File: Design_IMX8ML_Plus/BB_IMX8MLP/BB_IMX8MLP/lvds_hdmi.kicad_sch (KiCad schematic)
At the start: 4 parts, among them J15 LVDS0, J16 LVDS0, J7 HDMI_A, U2 HDMI2C1-14HDS

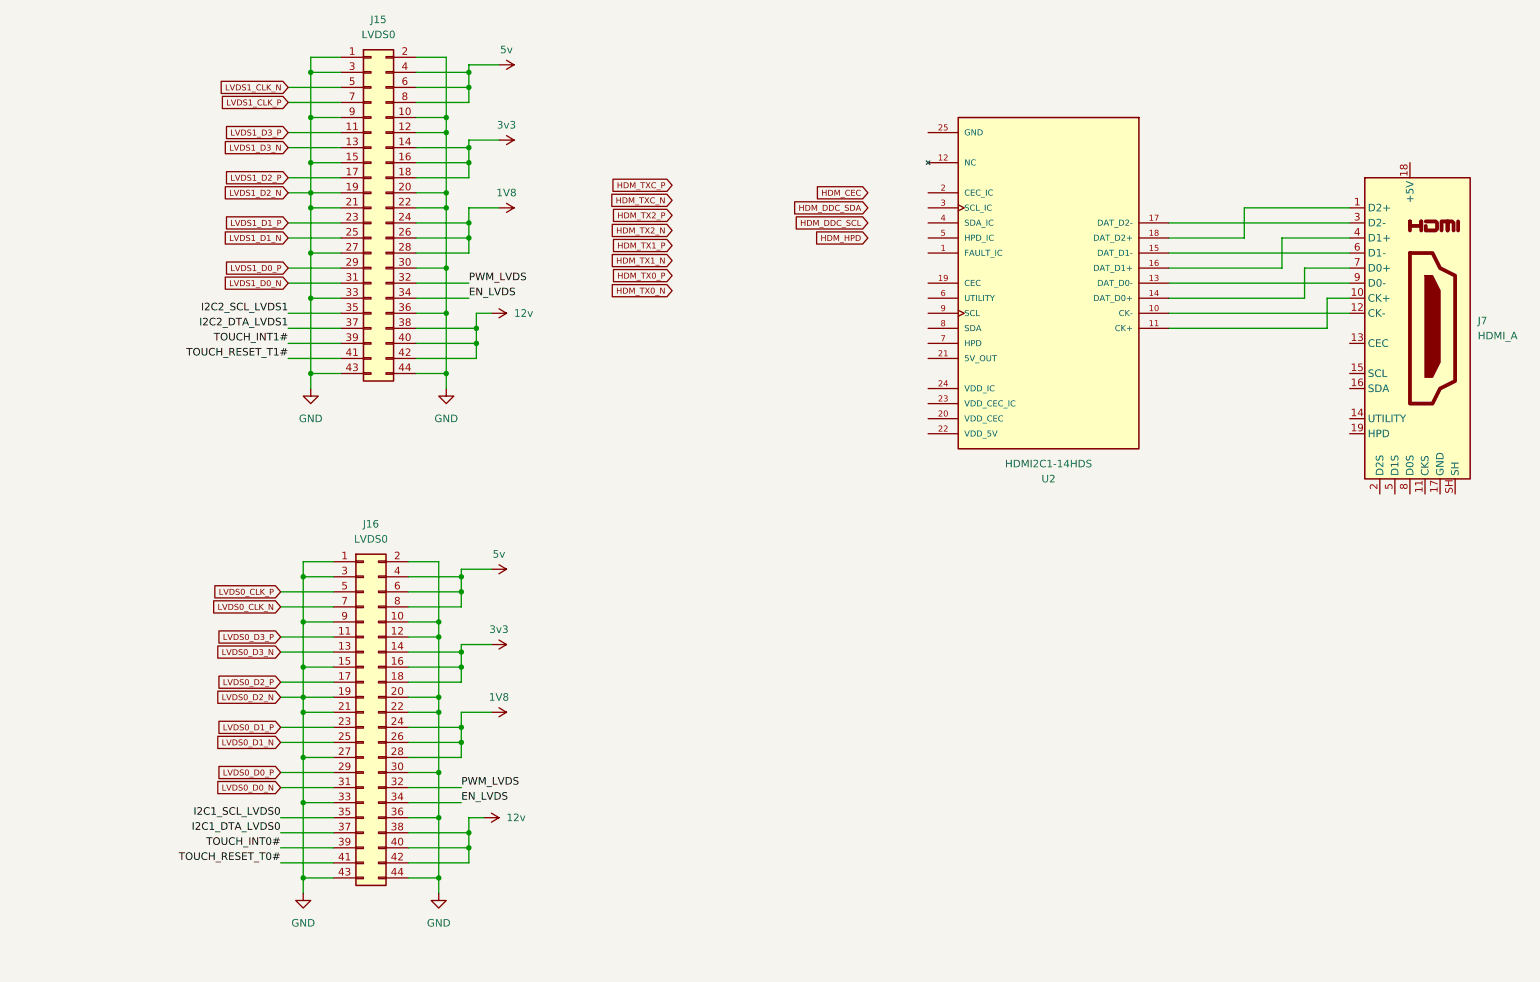
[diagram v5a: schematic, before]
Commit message: reorganization of the componentes
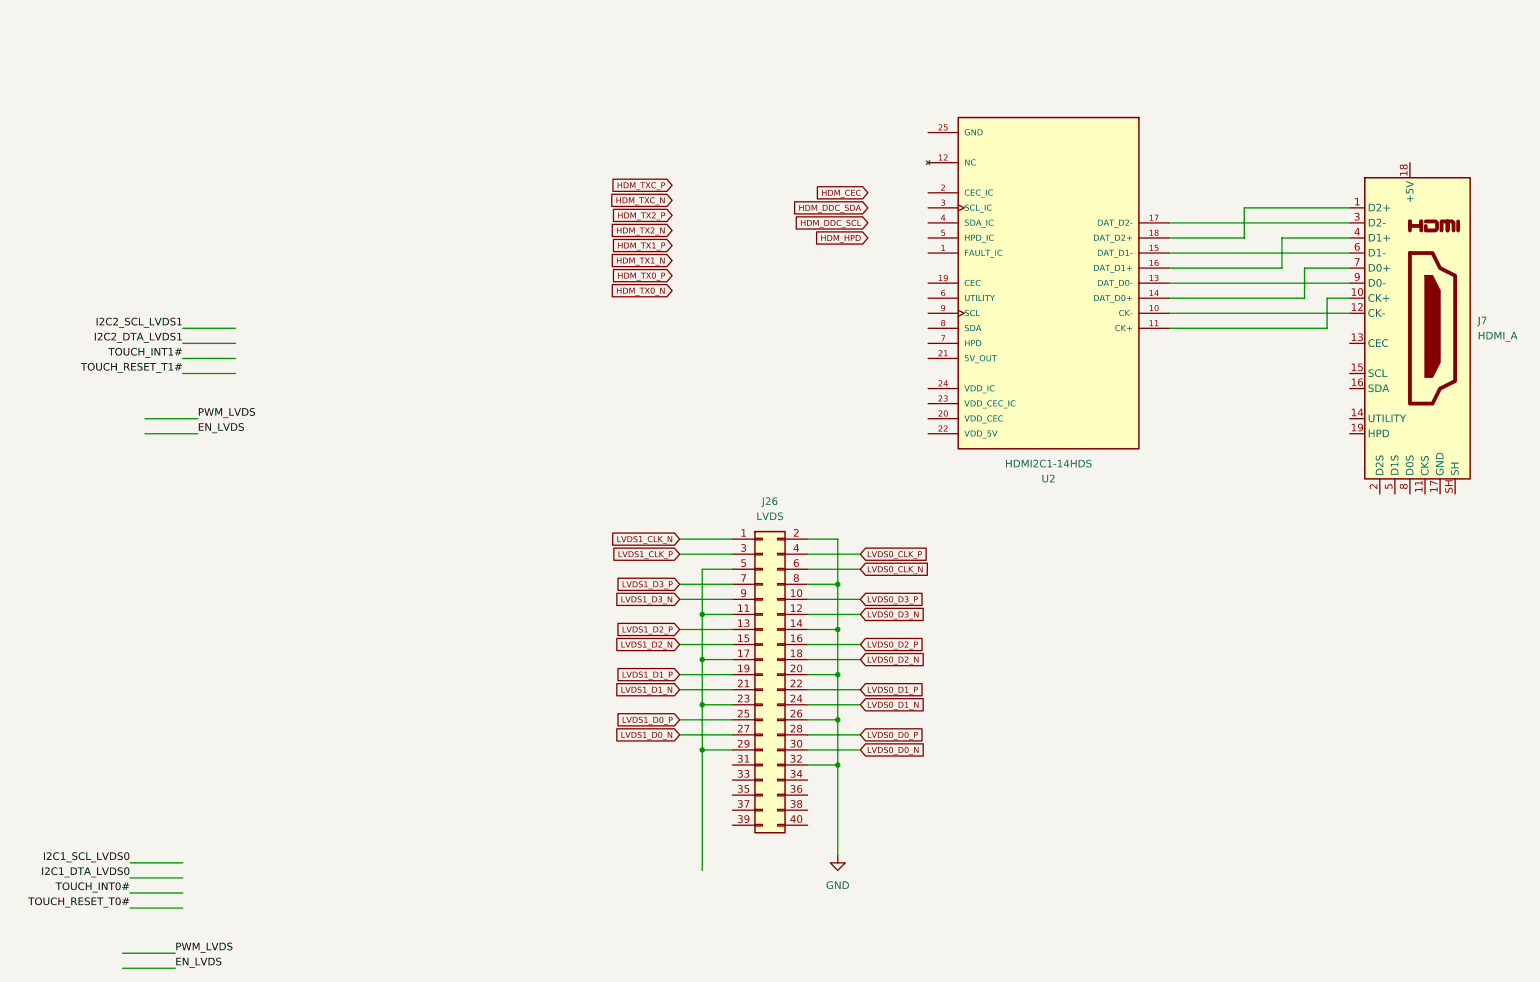
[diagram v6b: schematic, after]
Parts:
- removed J15, J16: LVDS0, symbol Connector_Generic:Conn_02x22_Odd_Even
- added J26: LVDS, Connector_PinHeader_1.00mm:PinHeader_2x20_P1.00mm_Vertical_SMD, symbol Connector_Generic:Conn_02x20_Odd_Even
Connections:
- net GND: now also J26.14 (Pin_14), J26.2 (Pin_2), J26.20 (Pin_20), J26.26 (Pin_26), J26.32 (Pin_32), J26.8 (Pin_8)
- net LVDS0_CLK_N: now also J26.6 (Pin_6)
- net LVDS0_CLK_P: now also J26.4 (Pin_4)
- net LVDS0_D0_N: now also J26.30 (Pin_30)
- net LVDS0_D0_P: now also J26.28 (Pin_28)
- net LVDS0_D1_N: now also J26.24 (Pin_24)
- net LVDS0_D1_P: now also J26.22 (Pin_22)
- net LVDS0_D2_P: now also J26.16 (Pin_16)
- net LVDS0_D3_N: now also J26.12 (Pin_12)
- net LVDS0_D3_P: now also J26.10 (Pin_10)
- net LVDS1_CLK_N: now also J26.1 (Pin_1)
- net LVDS1_CLK_P: now also J26.3 (Pin_3)
- net LVDS1_D0_N: now also J26.27 (Pin_27)
- net LVDS1_D0_P: now also J26.25 (Pin_25)
- net LVDS1_D1_N: now also J26.21 (Pin_21)
- net LVDS1_D1_P: now also J26.19 (Pin_19)
- net LVDS1_D2_P: now also J26.13 (Pin_13)
- net LVDS1_D3_N: now also J26.9 (Pin_9)
- net LVDS1_D3_P: now also J26.7 (Pin_7)
- new net: J26.11 (Pin_11), J26.17 (Pin_17), J26.23 (Pin_23), J26.29 (Pin_29), J26.5 (Pin_5)
- new net LVDS0_D2_N: J26.18 (Pin_18)
- new net LVDS1_D2_N: J26.15 (Pin_15)

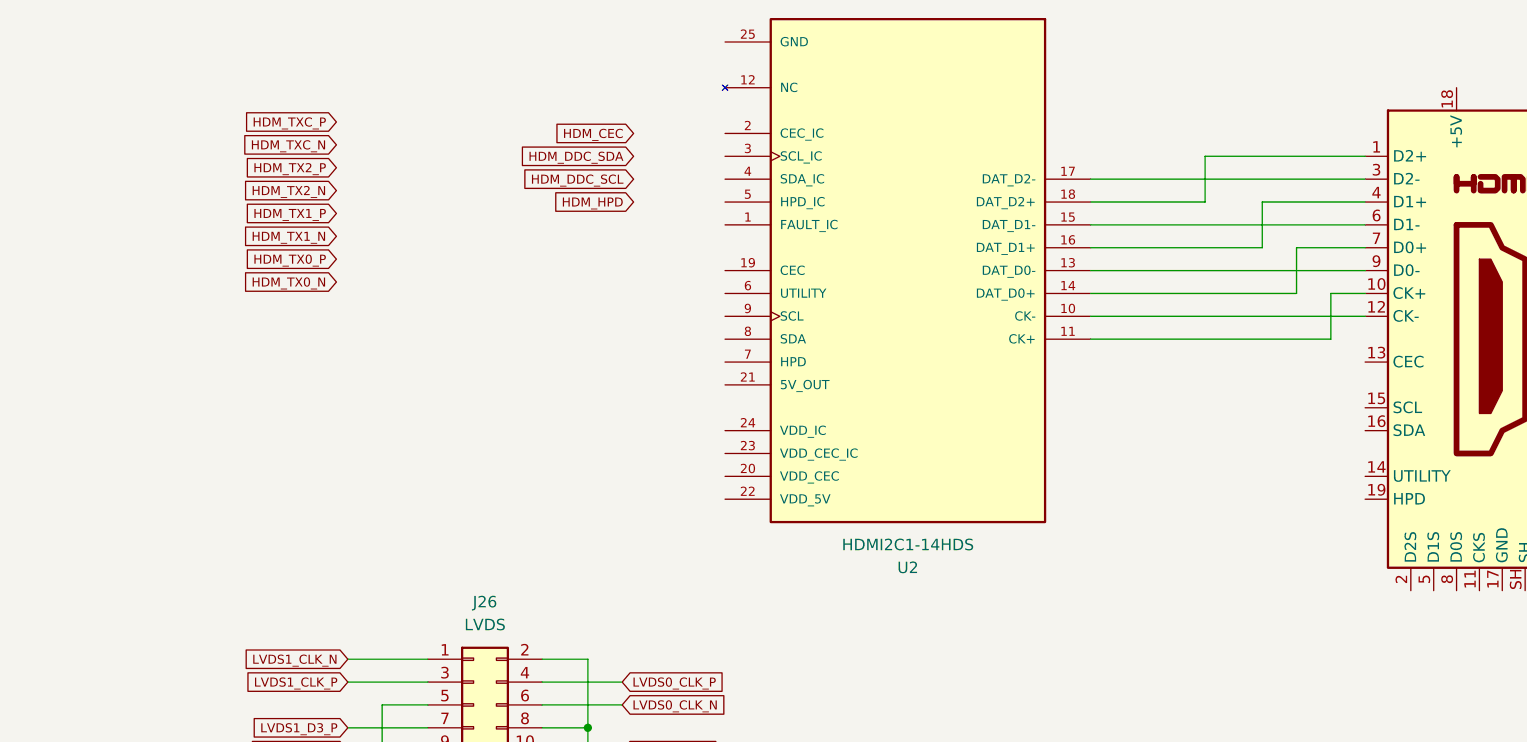
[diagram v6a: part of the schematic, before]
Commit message: Board base resize
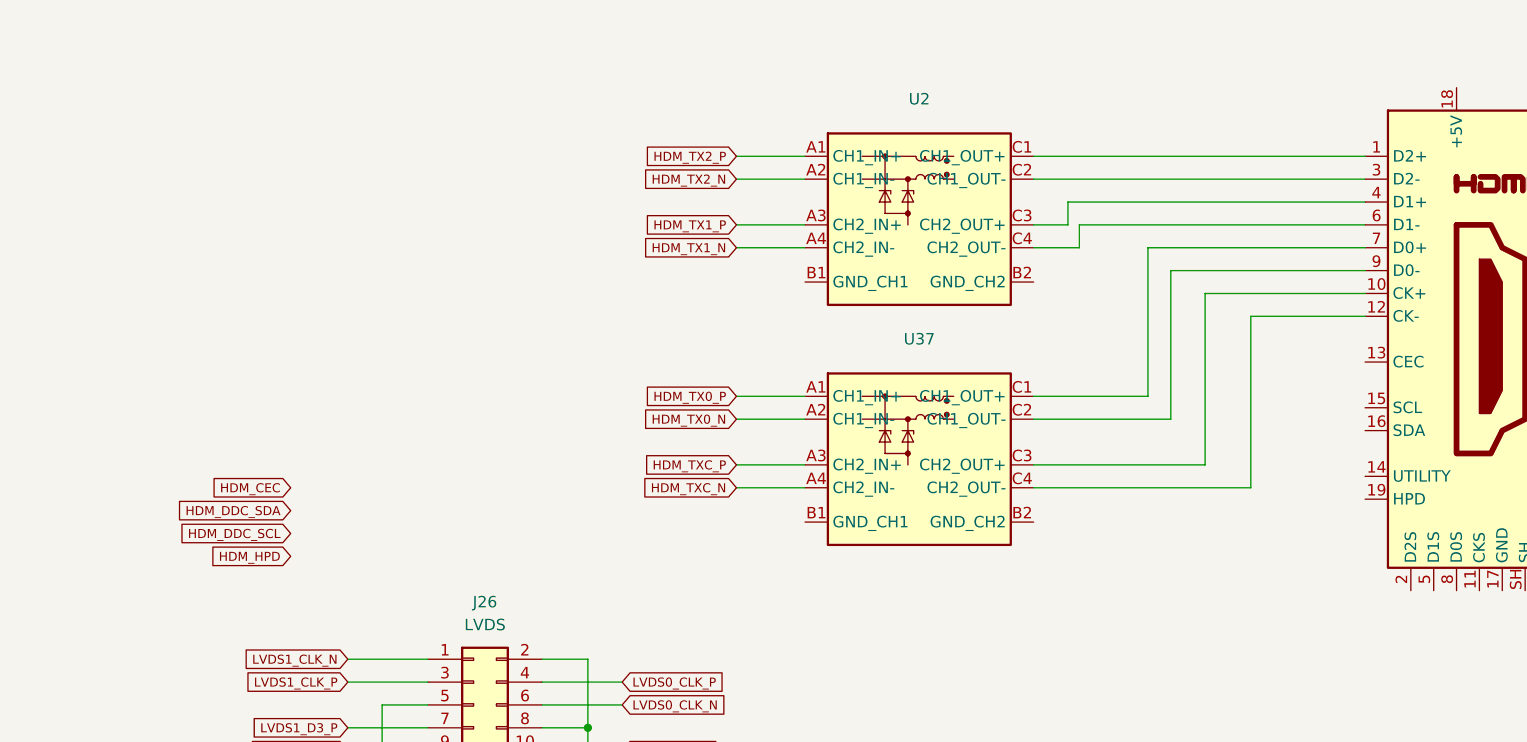
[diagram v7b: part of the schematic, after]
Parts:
- removed U2: HDMI2C1-14HDS, Package_DFN_QFN:VQFN-24-1EP_4x4mm_P0.5mm_EP2.5x2.5mm, symbol HDMI2C1-14HDS:HDMI2C1-14HDS
- added U2, U37: ~, _W_SBC:WLCSP10_4-2-4_NEX, symbol _W_MX8M:PCMF2HDMI12S
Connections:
- net HDM_TX0_N: now also U37.A2 (CH1_IN-)
- net HDM_TX0_P: now also U37.A1 (CH1_IN+)
- net HDM_TX1_N: now also U2.A4 (CH2_IN-)
- net HDM_TX1_P: now also U2.A3 (CH2_IN+)
- net HDM_TX2_N: now also U2.A2 (CH1_IN-)
- net HDM_TX2_P: now also U2.A1 (CH1_IN+)
- net HDM_TXC_N: now also U37.A4 (CH2_IN-)
- net HDM_TXC_P: now also U37.A3 (CH2_IN+)
- net at J7.1 (D2+): now also U2.C1 (CH1_OUT+)
- net at J7.10 (CK+): now also U37.C3 (CH2_OUT+)
- net at J7.12 (CK-): now also U37.C4 (CH2_OUT-)
- net at J7.3 (D2-): now also U2.C2 (CH1_OUT-)
- net at J7.4 (D1+): now also U2.C3 (CH2_OUT+)
- net at J7.6 (D1-): now also U2.C4 (CH2_OUT-)
- net at J7.7 (D0+): now also U37.C1 (CH1_OUT+)
- net at J7.9 (D0-): now also U37.C2 (CH1_OUT-)
